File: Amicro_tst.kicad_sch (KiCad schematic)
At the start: 39 parts, among them J1 Sensor, J2 Conn_01x05_Female, J3 Vibr, J4 Pow, J5 Screw_Terminal_01x02, Q1 Q_NPN_BEC, Q2 Q_NPN_BEC, Q3 Q_NPN_BEC, Q4 Q_NPN_BEC, SW1 RESET, U1 ATmega328-P, U2 24LC512, Y1 Crystal

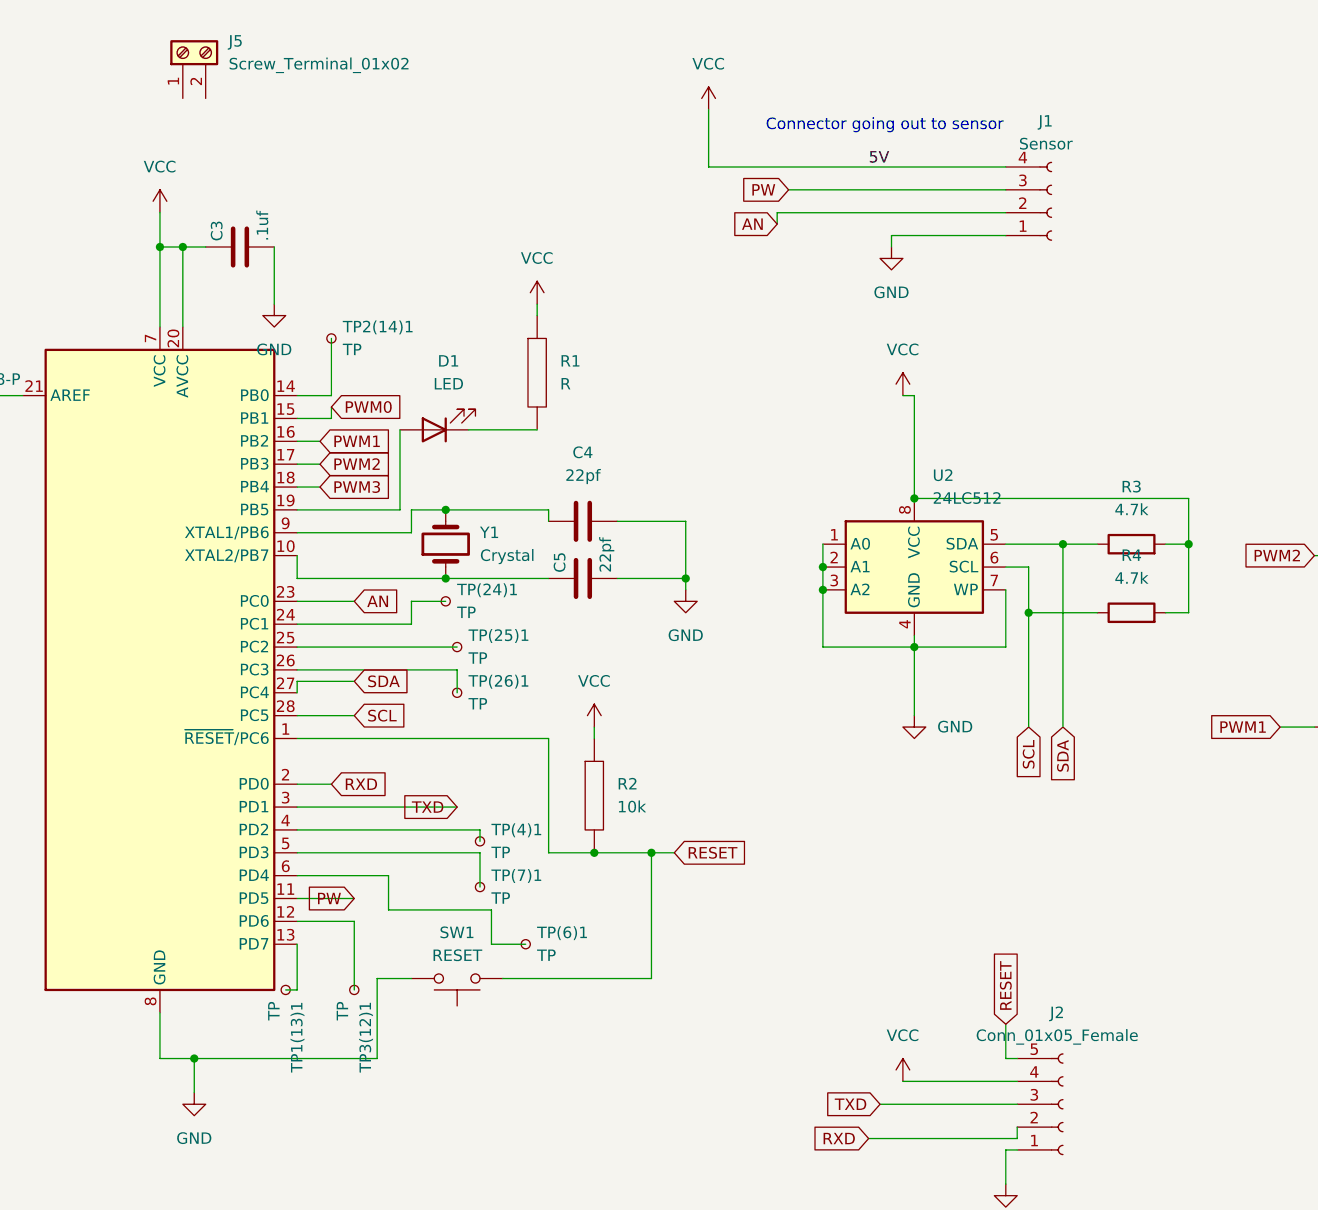
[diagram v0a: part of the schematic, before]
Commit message: Added ouline and lables
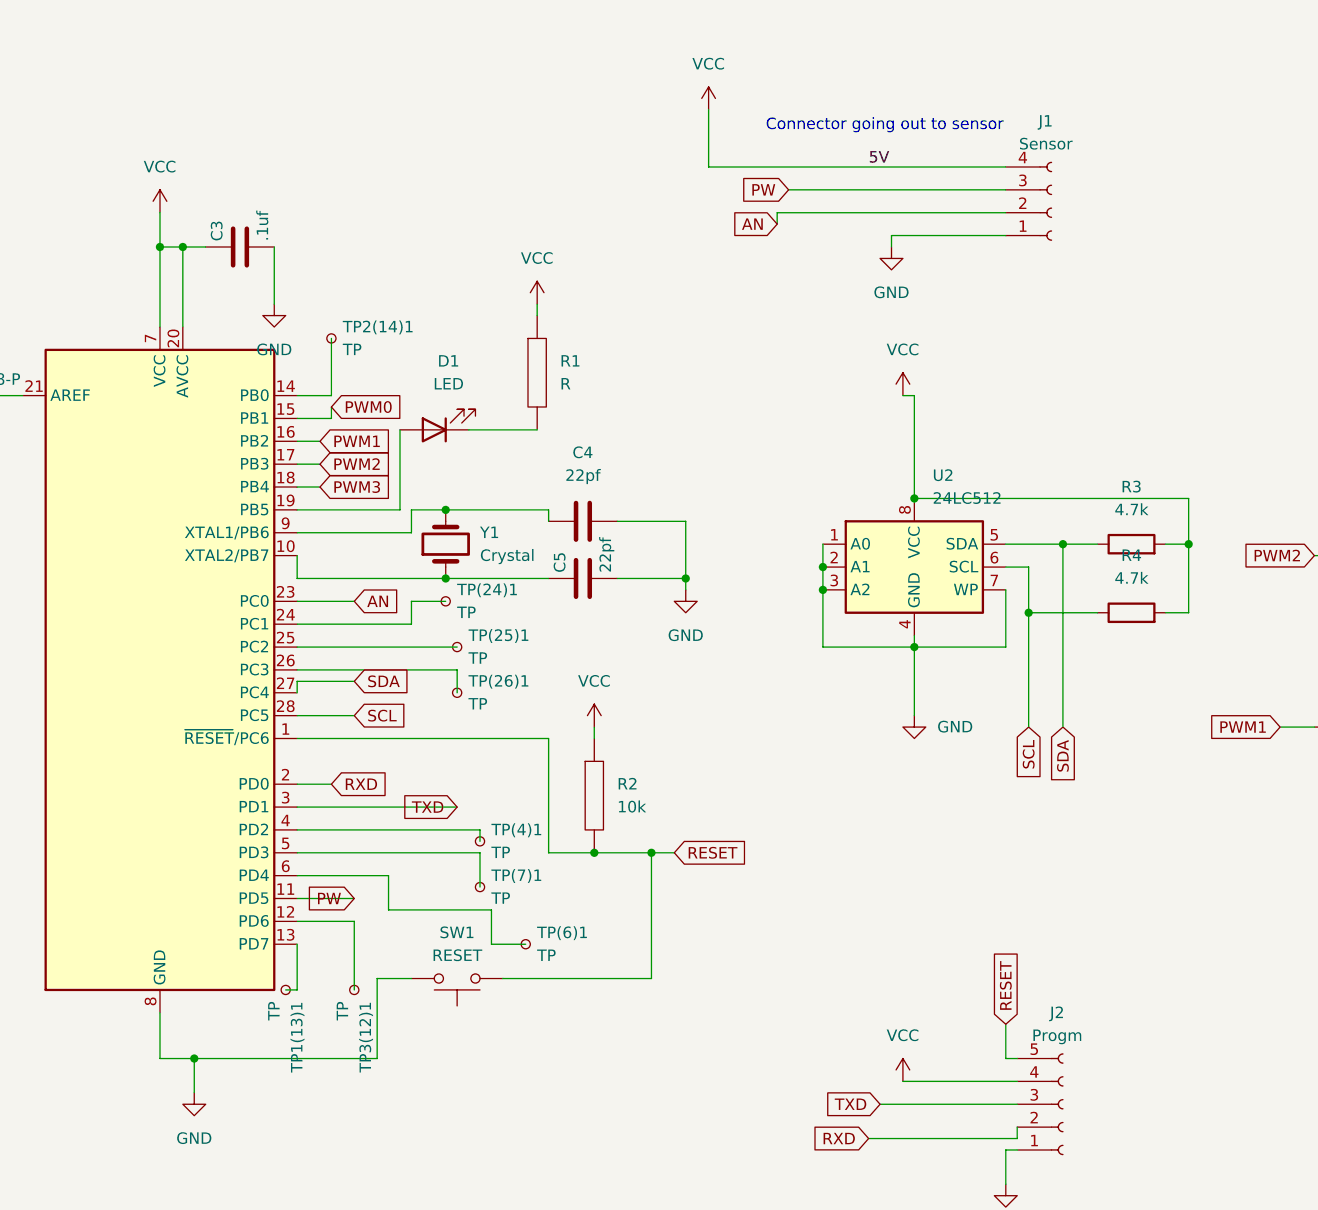
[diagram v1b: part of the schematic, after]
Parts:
- removed J5: Screw_Terminal_01x02, symbol Connector:Screw_Terminal_01x02
- J1: footprint Connector_JST:JST_EH_S4B-EH_1x04_P2.50mm_Horizontal -> Connector_JST:JST_EH_B4B-EH-A_1x04_P2.50mm_Vertical
- J2: value Conn_01x05_Female -> Progm
- J3: footprint (none) -> Connector_PinSocket_1.00mm:PinSocket_1x05_P1.00mm_Vertical
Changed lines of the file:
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@@
     (property "Reference" "J1" (id 0) (at 164.465 52.07 0))
     (property "Value" "Sensor" (id 1) (at 164.465 54.61 0))
-    (property "Footprint" "Connector_JST:JST_EH_S4B-EH_1x04_P2.50mm_Horizontal" (id 2) (at 165.1 62.23 0)
+    (property "Footprint" "Connector_JST:JST_EH_B4B-EH-A_1x04_P2.50mm_Vertical" (id 2) (at 165.1 62.23 0)
       (effects (font (size 1.27 1.27)) hide)
     )
@@
   (symbol (lib_id "power:VCC") (at 280.67 139.7 0) (unit 1)
     (in_bom yes) (on_board yes) (fields_autoplaced)
-    (property "Reference" "#PWR?" (id 0) (at 280.67 143.51 0)
+    (property "Reference" "#PWR0120" (id 0) (at 280.67 143.51 0)
       (effects (font (size 1.27 1.27)) hide)
     )
@@
       (effects (font (size 1.27 1.27)) (justify left))
     )
-    (property "Footprint" "" (id 2) (at 276.86 125.73 0)
+    (property "Footprint" "Connector_PinSocket_1.00mm:PinSocket_1x05_P1.00mm_Vertical" (id 2) (at 276.86 125.73 0)
       (effects (font (size 1.27 1.27)) hide)
     )
@@
     (pin "2")
   )
-  (symbol (lib_id "Connector:Screw_Terminal_01x02") (at 68.58 44.45 90) (unit 1)
-    (in_bom yes) (on_board yes) (fields_autoplaced)
-    (property "Reference" "J5" (id 0) (at 73.66 43.1799 90)
-      (effects (font (size 1.27 1.27)) (justify right))
-    )
-    (property "Value" "Screw_Terminal_01x02" (id 1) (at 73.66 45.7199 90)
-      (effects (font (size 1.27 1.27)) (justify right))
-    )
-    (property "Footprint" "" (id 2) (at 68.58 44.45 0)
-      (effects (font (size 1.27 1.27)) hide)
-    )
-    (property "Datasheet" "~" (id 3) (at 68.58 44.45 0)
-      (effects (font (size 1.27 1.27)) hide)
-    )
-    (pin "1")
-    (pin "2")
-  )
   (symbol (lib_id "power:VCC") (at 107.95 72.39 0) (unit 1)
     (in_bom yes) (on_board yes)
@@
     (in_bom yes) (on_board yes) (fields_autoplaced)
     (property "Reference" "J2" (id 0) (at 165.735 151.13 0))
-    (property "Value" "Conn_01x05_Female" (id 1) (at 165.735 153.67 0))
+    (property "Value" "Progm" (id 1) (at 165.735 153.67 0))
     (property "Footprint" "Connector_PinSocket_1.00mm:PinSocket_1x05_P1.00mm_Vertical" (id 2) (at 166.37 161.29 0)
       (effects (font (size 1.27 1.27)) hide)
@@
     )
     (path "/67c38179-7cf7-4029-aa2e-cf868ebc3e94"
-      (reference "#PWR?") (unit 1) (value "VCC") (footprint "")
+      (reference "#PWR0120") (unit 1) (value "VCC") (footprint "")
     )
     (path "/fb0aa499-1a5b-46b6-b9de-14c9c6464288"
@@
     )
     (path "/5188af90-2c2e-4efc-b1a8-f03acba966ff"
-      (reference "J1") (unit 1) (value "Sensor") (footprint "Connector_JST:JST_EH_S4B-EH_1x04_P2.50mm_Horizontal")
+      (reference "J1") (unit 1) (value "Sensor") (footprint "Connector_JST:JST_EH_B4B-EH-A_1x04_P2.50mm_Vertical")
     )
     (path "/fabc0f20-6748-4256-8270-8d8c1ba7f1db"
-      (reference "J2") (unit 1) (value "Conn_01x05_Female") (footprint "Connector_PinSocket_1.00mm:PinSocket_1x05_P1.00mm_Vertical")
+      (reference "J2") (unit 1) (value "Progm") (footprint "Connector_PinSocket_1.00mm:PinSocket_1x05_P1.00mm_Vertical")
     )
     (path "/d06bff60-dd66-4461-a791-89966a79340a"
-      (reference "J3") (unit 1) (value "Vibr") (footprint "")
+      (reference "J3") (unit 1) (value "Vibr") (footprint "Connector_PinSocket_1.00mm:PinSocket_1x05_P1.00mm_Vertical")
     )
     (path "/b3060f11-28e1-4ef4-8cb3-348282790846"
       (reference "J4") (unit 1) (value "Pow") (footprint "TestPoint:TestPoint_2Pads_Pitch5.08mm_Drill1.3mm")
     )
-    (path "/d9983f71-6b47-4585-9513-3514b250772e"
-      (reference "J5") (unit 1) (value "Screw_Terminal_01x02") (footprint "")
-    )
     (path "/c9e48f35-9002-4ee0-bbbf-ca80e2ff2954"
